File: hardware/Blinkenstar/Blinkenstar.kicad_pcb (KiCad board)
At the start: 2 copper layers, 84.4 x 82.8 mm, 19 parts, among them U1 TINY48/88B, U2 EEPROM-I2CEIAJ

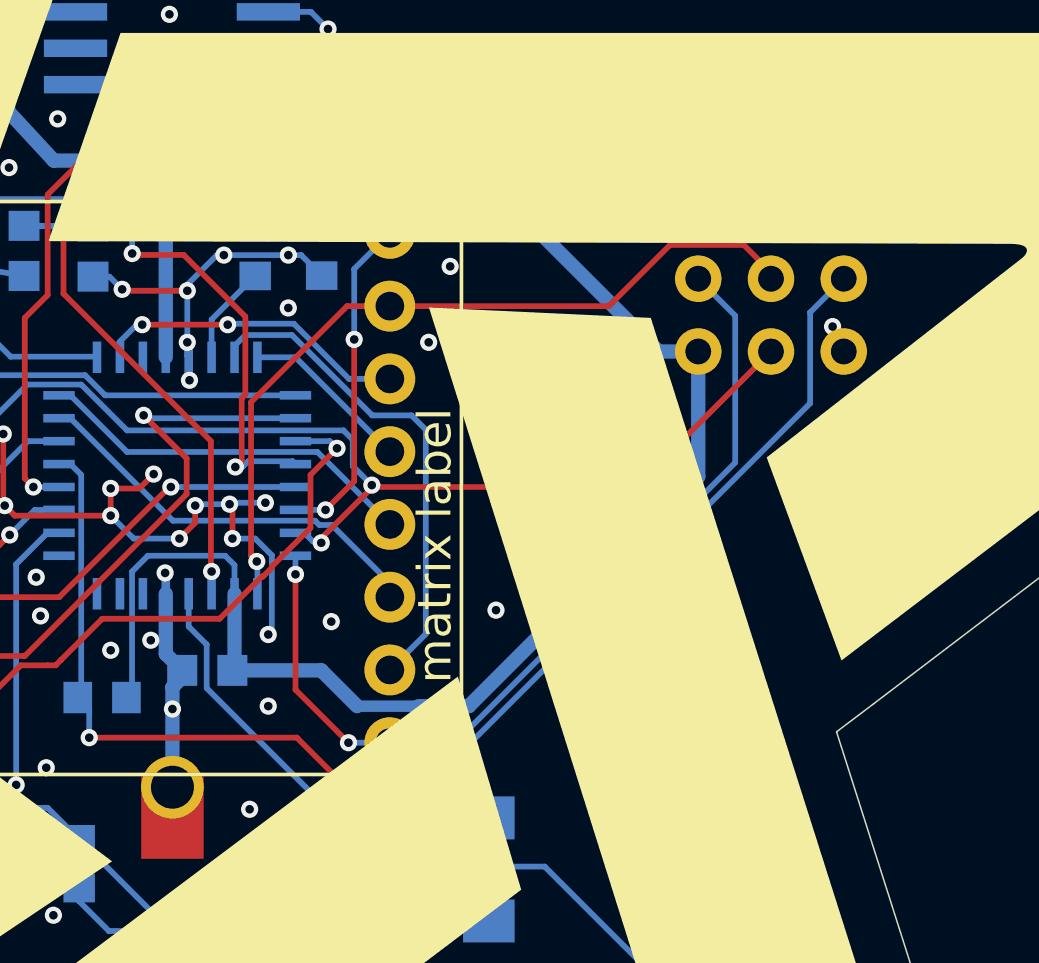
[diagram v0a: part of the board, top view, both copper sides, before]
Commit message: better ICSP layout
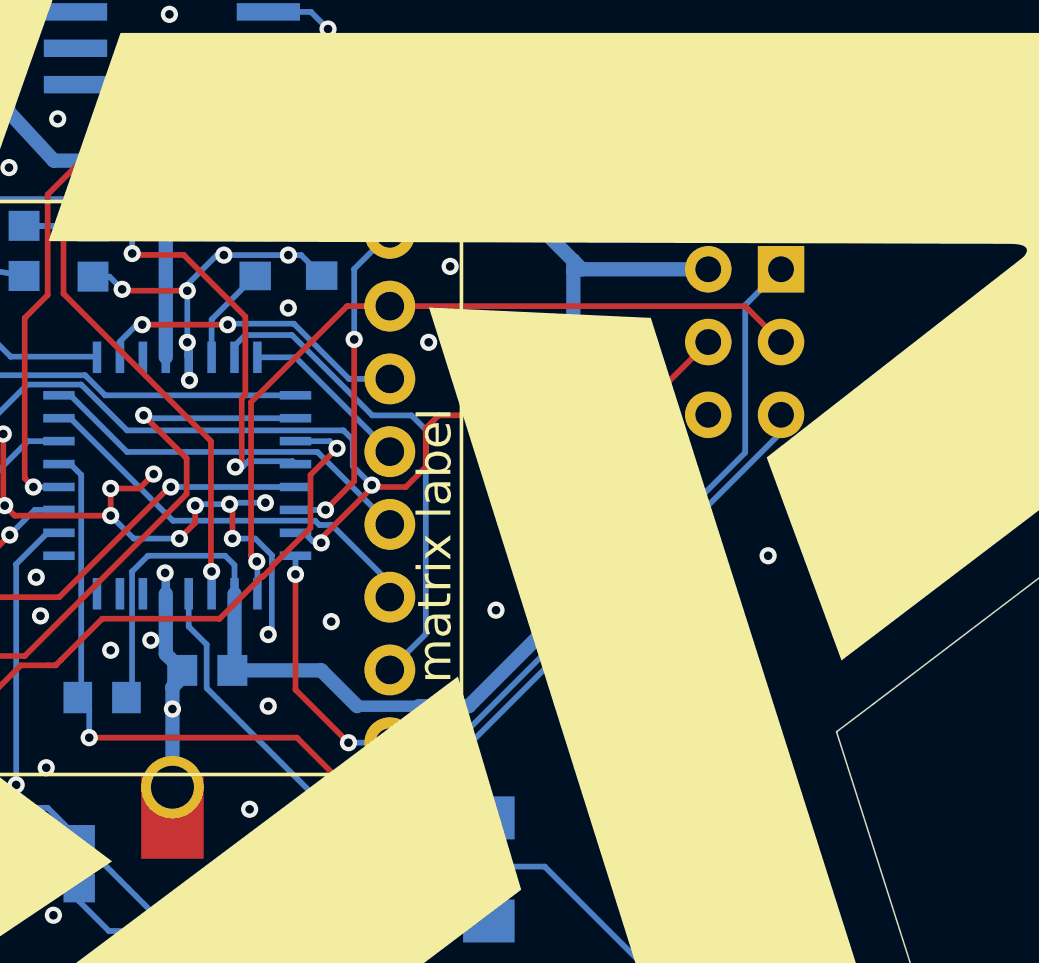
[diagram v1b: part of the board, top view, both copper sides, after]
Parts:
- moved ISP1 1.32 mm to (134.7, 84.3), turned to 180 degrees
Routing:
- net RESET: track 46.6 -> 41.0 mm
- net VCC: track 80.6 -> 81.9 mm
- net /R4/MOSI: track 37.3 -> 36.2 mm
- net /R6/SCK: track 28.2 -> 27.6 mm
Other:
- board text added: "+VCC MOSI GND"
- board text added: "ICSP"
- board text added: "MISO SCK Reset"
- board text added: "v2.6"
- board text removed: "v2.5"

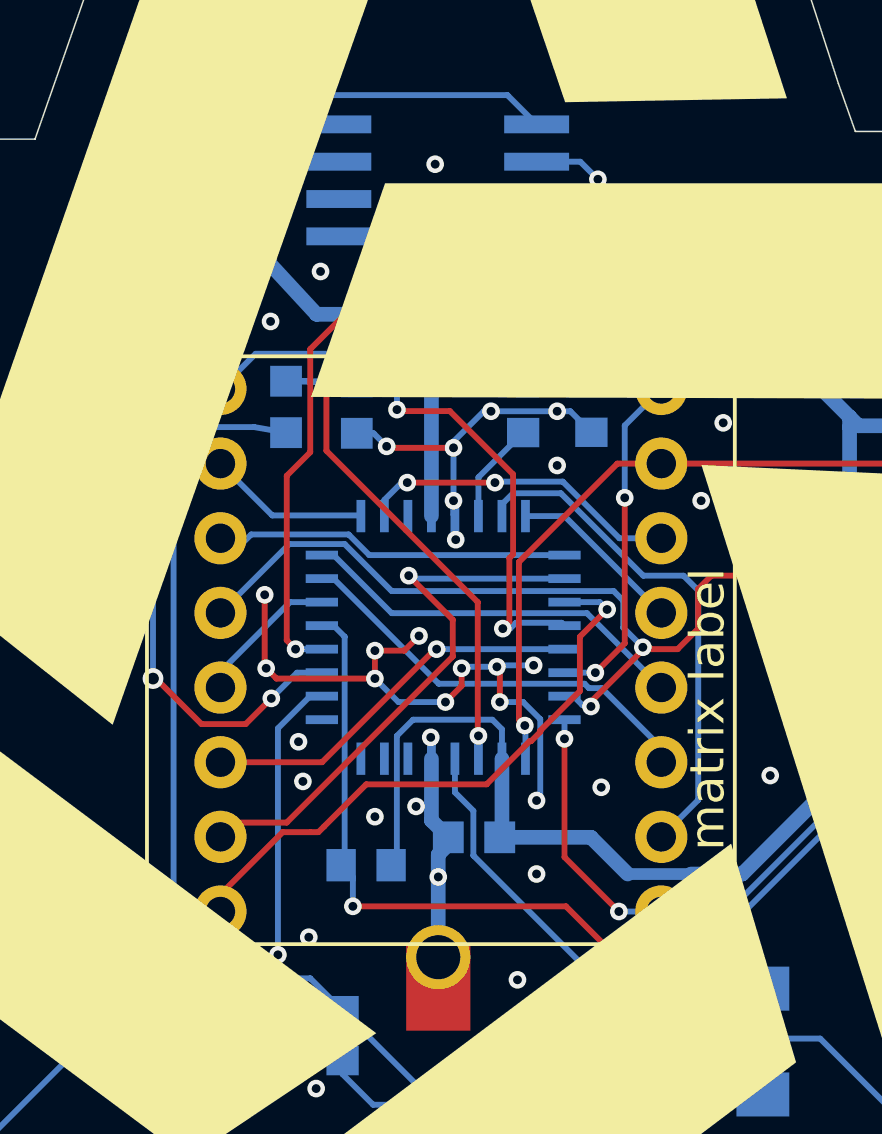
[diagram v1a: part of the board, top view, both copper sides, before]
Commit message: enhance pad size for MCU soldering
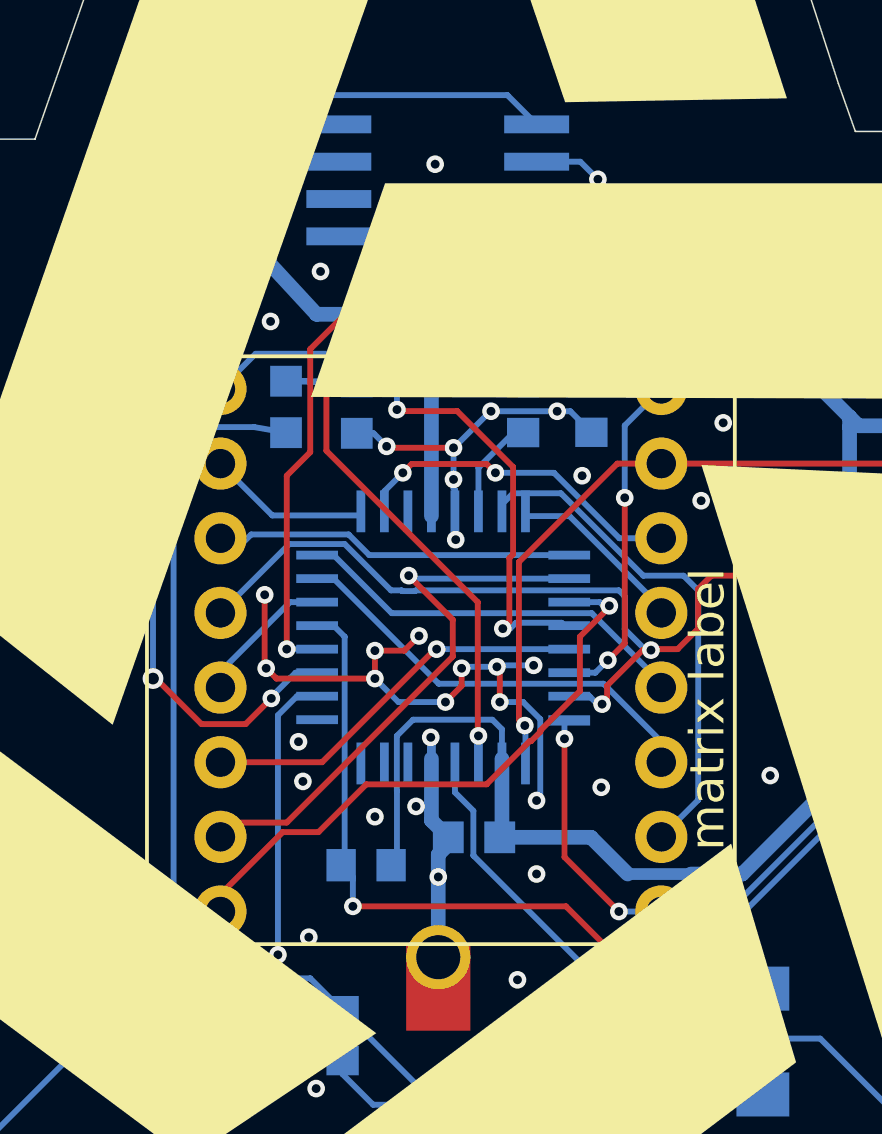
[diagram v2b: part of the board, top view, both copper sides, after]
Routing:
- net /C5: track 11.0 -> 11.7 mm

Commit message: WIP
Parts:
- removed U$5: CR2032_ELECTRODRAGON, minirocket_2.4:CR2032PAC_ELECTRODRAGON
- removed U1: TINY48/88B, minirocket_2.4:TQFP32-08
- added BT1: Battery_Cell, Library:CR2032PAC_ELECTRODRAGON, B.Cu at (114.8, 89.3)
- added J1: AudioJack2_Ground, Library:AUDIO-JACK, B.Cu at (114.8, 112.3)
- added JP2: PINHD-1X04_2.54-S, Connector_PinHeader_1.00mm:PinHeader_1x04_P1.00mm_Vertical, B.Cu at (97.3, 101.6)
- added U3: EEPROM-I2CEIAJ, Package_SO:SOIC-8_3.9x4.9mm_P1.27mm, B.Cu at (114.7, 73.4)
- C1, C2, C3: footprint minirocket_2.4:C0603K -> Capacitor_SMD:C_0603_1608Metric_Pad1.08x0.95mm_HandSolder
- D1, D2: value 1N4148 -> 1N4148W; footprint minirocket_2.4:SOD3718X135N -> Diode_SMD:D_SOD-123
- ISP1: value AVRISP-6 -> AVR-ISP-6VERT; footprint minirocket_2.4:AVRISP -> Connector_PinHeader_2.54mm:PinHeader_2x03_P2.54mm_Vertical
- JP1: value AUDIO-JACKPTH -> PINHD-1X04_2.54-S; footprint minirocket_2.4:AUDIO-JACK -> Connector_PinHeader_1.00mm:PinHeader_1x04_P1.00mm_Vertical
- LED1: value SEGMENT_8X8_ROWCATHODEMINIDISPLAY -> SEGMENT_8X8_ROWCATHODEM12A881UR; footprint minirocket_2.4:SEGMENT_BL-M12A883 -> Library:SEGMENT_BL-M12A883
- R1: value 8.2K -> 16; footprint minirocket_2.4:R0603 -> Resistor_SMD:R_0603_1608Metric_Pad0.98x0.95mm_HandSolder
- R2: value 6.8K -> 8.2K; footprint minirocket_2.4:R0603 -> Resistor_SMD:R_0603_1608Metric_Pad0.98x0.95mm_HandSolder
- R3: value 16 -> 6.8K; footprint minirocket_2.4:R0603 -> Resistor_SMD:R_0603_1608Metric_Pad0.98x0.95mm_HandSolder
- R4, R5, R6: footprint minirocket_2.4:R0603 -> Resistor_SMD:R_0603_1608Metric_Pad0.98x0.95mm_HandSolder
- S1, S2: value 10-XX -> B3F-1000; footprint minirocket_2.4:B3F-10XX -> Library:B3F-10XX
- U2: value EEPROM-I2CEIAJ -> ATtiny88-A; footprint minirocket_2.4:SO08-EIAJ -> Package_QFP:TQFP-32_7x7mm_P0.8mm
- moved S2 47.2 mm to (91.0, 121.5)
- moved S1 47.2 mm to (138.2, 121.3)
- moved JP1 36.5 mm to (98.5, 79.7), turned to -17 degrees
- moved R3 23.0 mm to (119.9, 81.2), turned to 90 degrees
- moved R1 22.2 mm to (111.5, 102.6)
- moved R6 22.0 mm to (108.7, 75.0), turned to 90 degrees
- moved R4 21.9 mm to (112.2, 96.8), turned to 0 degrees
- moved U2 15.6 mm to (114.9, 89.0), turned to -90 degrees
- moved ISP1 2.84 mm to (135.9, 81.8)
- moved R2 2.32 mm to (117.6, 81.2), turned to -90 degrees
- moved LED1 0.08 mm to (114.9, 89.4)
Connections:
- C1 pad 1: Net-(C1-Pad1) -> Net-(D1-A)
- ISP1 pad 5: RESET -> /RESET
- R1 pad 1: /AVR_AUDIO_IN -> Net-(D1-A)
- R1 pad 2: /TRIG2 -> Net-(J1-PadS)
- R2 pad 1: GND -> /AVR_AUDIO_IN
- R2 pad 2: /AVR_AUDIO_IN -> /TRIG2
- R3 pad 1: Net-(C1-Pad1) -> GND
- R3 pad 2: Net-(JP1-RIGHT) -> /AVR_AUDIO_IN
- R4 pad 1: VCC -> /RESET
- R4 pad 2: SDA -> VCC
- R5 pad 2: SCL -> /SCL
- R6 pad 2: RESET -> /SDA
- S1 pad 1: /B2 -> /B1
- S2 pad 1: /B1 -> /B2
- U2 pad 1: GND -> /C4
- U2 pad 2: GND -> /C5
- U2 pad 3: GND -> /TRIG1
- U2 pad 4: GND -> VCC
- U2 pad 5: SDA -> GND
- U2 pad 6: SCL -> /TRIG2
- U2 pad 7: GND -> /R7
- U2 pad 8: VCC -> /R8
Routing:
- net Net-(D1-A): track 0.00 -> 45.5 mm
- net Net-(C1-Pad1): track 45.1 -> 0.00 mm
- net /RESET: track 0.00 -> 41.1 mm, vias 0 -> 2
- net RESET: track 41.0 -> 0.00 mm, vias 2 -> 0
- net SDA: track 38.3 -> 0.00 mm, vias 2 -> 0
- net /SDA: track 0.00 -> 37.4 mm, vias 0 -> 2
- net VCC: track 81.9 -> 118.6 mm, vias 0 -> 2
- net /E2: track 0.00 -> 32.7 mm, vias 0 -> 2
- net SCL: track 29.9 -> 0.00 mm, vias 2 -> 0
- net /SCL: track 0.00 -> 29.9 mm, vias 0 -> 2
- net /E1: track 0.00 -> 28.3 mm, vias 0 -> 2
- net /E4: track 0.00 -> 24.7 mm, vias 0 -> 2
- net /E3: track 0.00 -> 23.5 mm, vias 0 -> 2
- net GND: track 42.6 -> 29.4 mm, vias 37 -> 44
- net Net-(J1-PadS): track 0.00 -> 10.7 mm
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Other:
- board text added: "Back side!"
- board text added: "v2.7"
- board text removed: "v2.6"

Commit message: WIP
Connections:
- BT1 pad +: (no net) -> VCC
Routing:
- net VCC: track 118.6 -> 119.9 mm, vias 2 -> 3
- net GND: vias 44 -> 70
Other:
- board text added: "DATA"

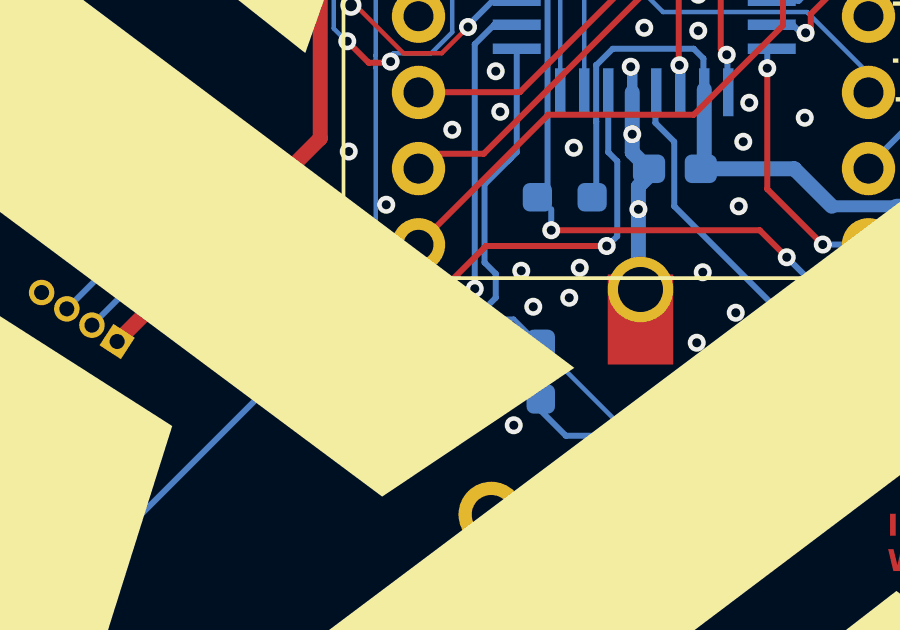
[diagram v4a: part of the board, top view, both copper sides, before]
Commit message: fix GND issue
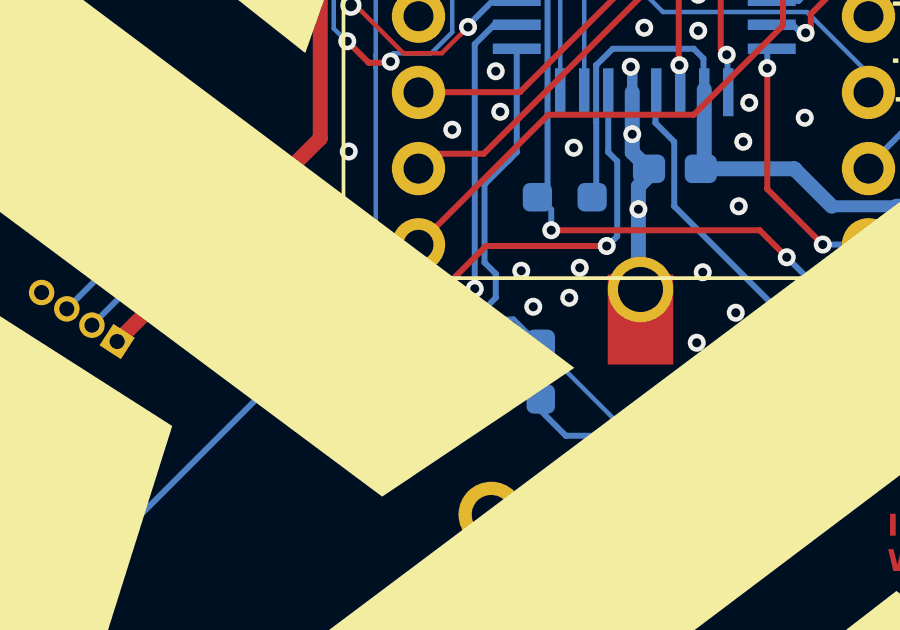
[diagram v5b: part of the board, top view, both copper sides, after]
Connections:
- BT1 pad +: VCC -> (no net)
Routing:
- net GND: vias 70 -> 69
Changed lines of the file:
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@@
 			(psa4output no)
 			(plot_black_and_white yes)
-			(plotinvisibletext no)
 			(sketchpadsonfab no)
 			(plotpadnumbers no)
@@
 		(sheetname "/")
 		(sheetfile "Blinkenstar.kicad_sch")
-		(attr exclude_from_pos_files exclude_from_bom dnp)
+		(attr exclude_from_pos_files)
 		(fp_line
 			(start 10 -10)
@@
 		(sheetname "/")
 		(sheetfile "Blinkenstar.kicad_sch")
-		(attr exclude_from_pos_files exclude_from_bom dnp)
+		(attr exclude_from_pos_files)
 		(fp_line
 			(start -1.27 3.048)
@@
 		(sheetname "/")
 		(sheetfile "Blinkenstar.kicad_sch")
-		(attr exclude_from_pos_files exclude_from_bom dnp)
+		(attr exclude_from_pos_files)
 		(fp_line
 			(start -1.27 3.048)
@@
 		(sheetname "/")
 		(sheetfile "Blinkenstar.kicad_sch")
-		(attr exclude_from_pos_files exclude_from_bom dnp)
+		(attr exclude_from_pos_files)
 		(fp_line
 			(start -7 3.81)
@@
 			(layers "*.Cu" "*.Mask")
 			(remove_unused_layers no)
-			(net 1 "VCC")
 			(solder_mask_margin 0.0508)
 			(thermal_bridge_angle 0)
@@
 		(sheetname "/")
 		(sheetfile "Blinkenstar.kicad_sch")
-		(attr through_hole exclude_from_pos_files exclude_from_bom dnp)
+		(attr through_hole exclude_from_pos_files)
 		(fp_line
 			(start -0.695001 0.684998)
@@
 		(sheetname "/")
 		(sheetfile "Blinkenstar.kicad_sch")
-		(attr through_hole exclude_from_pos_files exclude_from_bom dnp)
+		(attr through_hole exclude_from_pos_files)
 		(fp_line
 			(start -0.695001 -3.560005)
@@
 		(sheetname "/")
 		(sheetfile "Blinkenstar.kicad_sch")
-		(attr through_hole exclude_from_pos_files exclude_from_bom dnp)
+		(attr through_hole exclude_from_pos_files)
 		(fp_line
 			(start 3.87 1.33)
@@
 		(sheetname "/")
 		(sheetfile "Blinkenstar.kicad_sch")
-		(attr exclude_from_pos_files exclude_from_bom dnp)
+		(attr exclude_from_pos_files)
 		(fp_line
 			(start 7.5 -6)
@@
 	)
 	(via
-		(at 106.3 97)
-		(size 0.6)
-		(drill 0.3)
-		(layers "F.Cu" "B.Cu")
-		(net 2)
-	)
-	(via
 		(at 112.75 99.1)
 		(size 0.6)
@@
 	)
 	(via
-		(at 110.55 104.35)
+		(at 109.33 103.71)
 		(size 0.6)
 		(drill 0.3)
@@
 		(min_thickness 0.25)
 		(filled_areas_thickness no)
-		(fill yes
+		(fill
 			(thermal_gap 0.5)
 			(thermal_bridge_width 0.5)
@@
 		(min_thickness 0.25)
 		(filled_areas_thickness no)
-		(fill yes
+		(fill
 			(thermal_gap 0.5)
 			(thermal_bridge_width 0.5)
